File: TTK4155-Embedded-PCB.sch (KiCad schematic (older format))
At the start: 48 parts, among them J1 AVR-JTAG-10, J2 DB9_Female, J3 Conn_01x10_Male, J4 Conn_01x04_Male, J5 Screw_Terminal_01x02, J6 Screw_Terminal_01x02, J7 Conn_01x04_Male, J8 BannanaJack, SW1 SW_Push, U1 L7805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

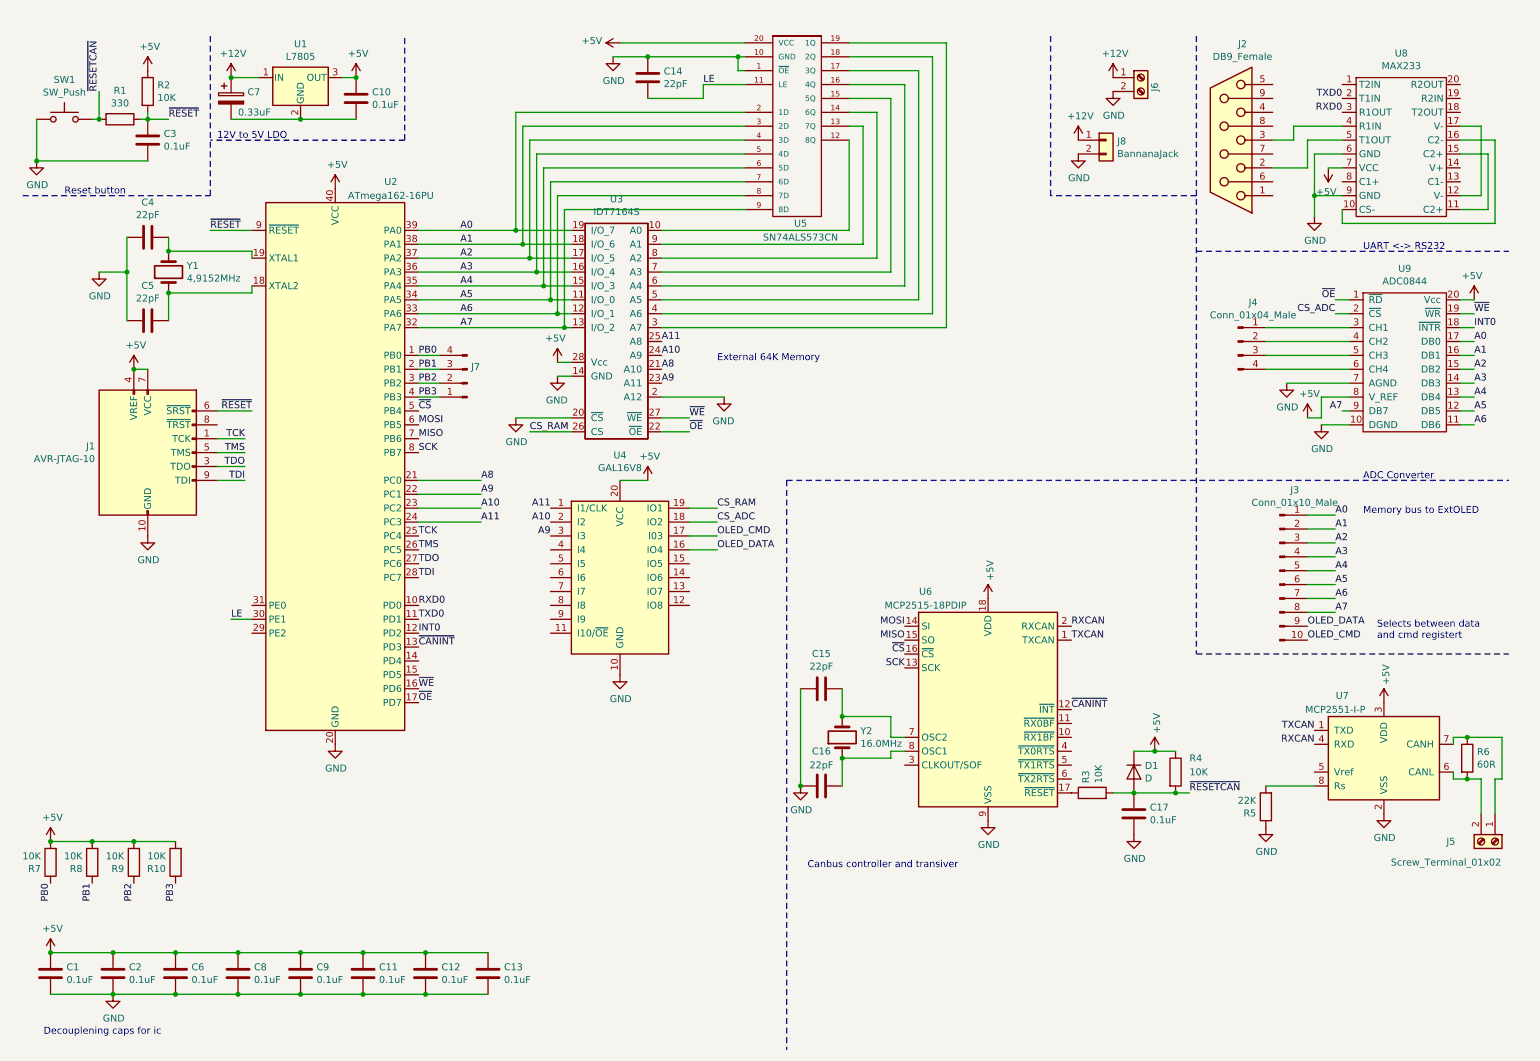
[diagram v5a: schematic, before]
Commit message: Fixed schematics to reflects bodges in rev 1
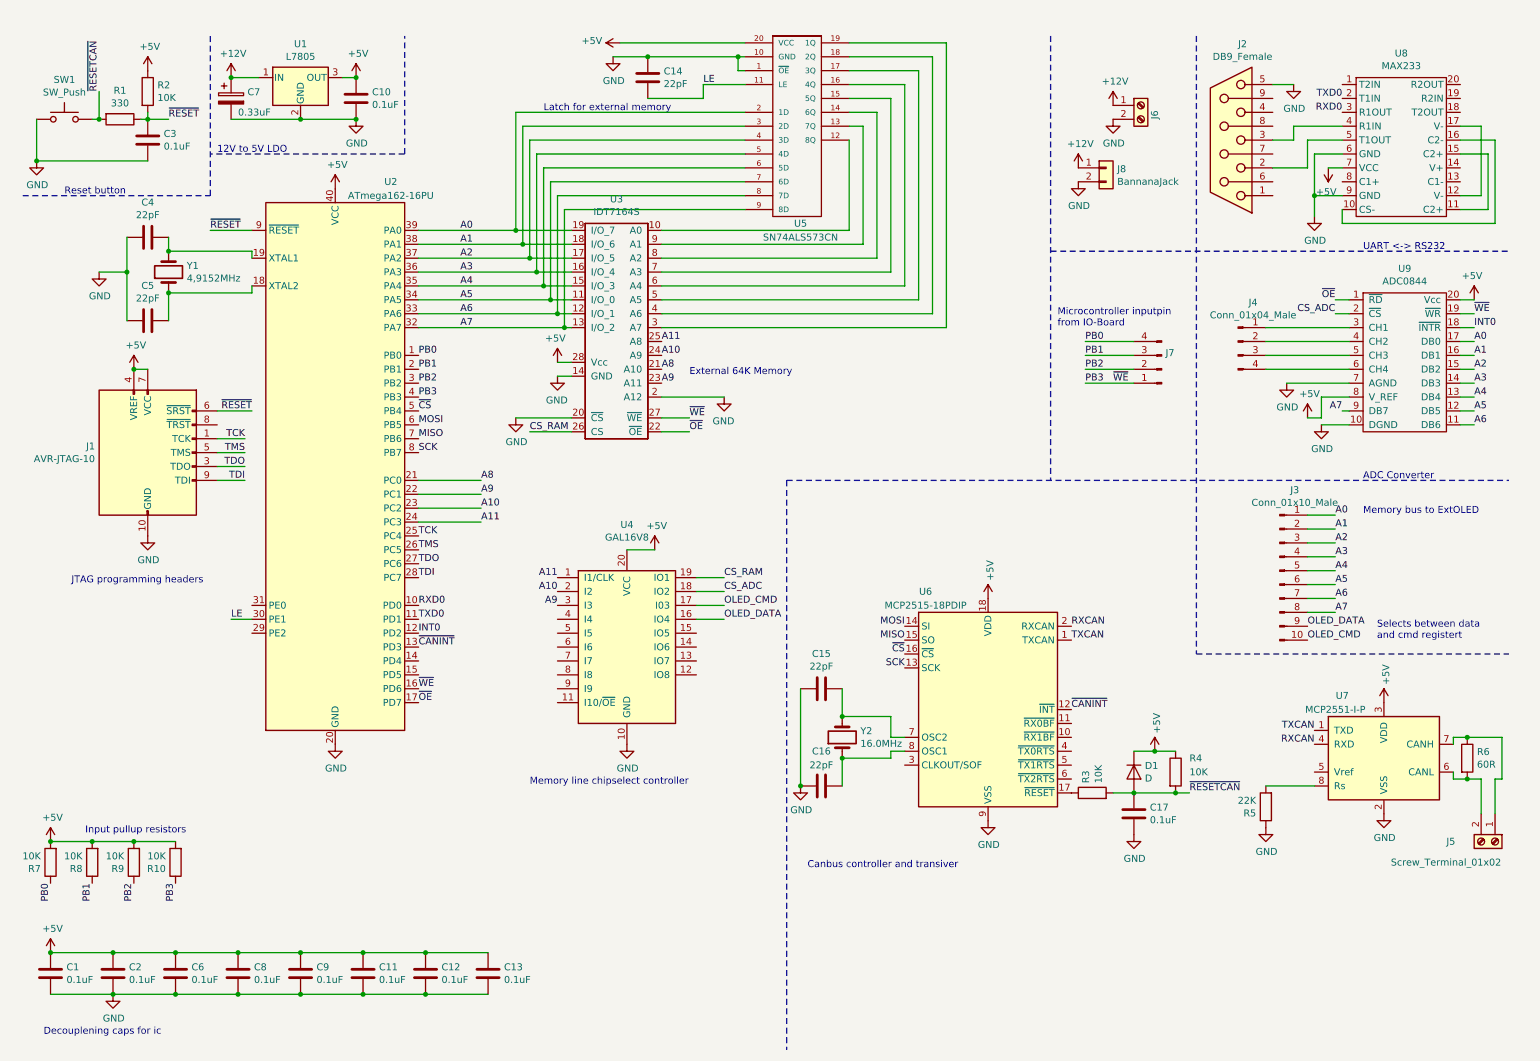
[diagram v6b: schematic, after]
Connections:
- net ~WE is gone; now on net PB3: U2.16 (PD6), U3.27 (~WE), U9.19 (~WR)
- net GND: now also C10.2, C7.2, J2.5, U1.2 (GND)
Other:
- note added: "Input pullup resistors"
- note added: "JTAG programming headers"
- note added: "Latch for external memory"
- note added: "Memory line chipselect controller\n"
- note added: "Microcontroller inputpin \nfrom IO-Board"
- moved on the sheet: J6, J7, J8, U4
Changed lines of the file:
@@
 EESchema Schematic File Version 4
 LIBS:TTK4155-Embedded-PCB-cache
-EELAYER 29 0
+EELAYER 30 0
 EELAYER END
 $Descr A4 11693 8268
@@
 L power:+5V #PWR0116
 U 1 1 5D9B7D1E
-P 5000 3700
-F 0 "#PWR0116" H 5000 3550 50  0001 C CNN
-F 1 "+5V" H 5015 3873 50  0000 C CNN
-F 2 "" H 5000 3700 50  0001 C CNN
-F 3 "" H 5000 3700 50  0001 C CNN
-	1    5000 3700
-	1    0    0    -1
-$EndComp
-Wire Wire Line
-	5500 3900 5300 3900
+P 5050 4200
+F 0 "#PWR0116" H 5050 4050 50  0001 C CNN
+F 1 "+5V" H 5065 4373 50  0000 C CNN
+F 2 "" H 5050 4200 50  0001 C CNN
+F 3 "" H 5050 4200 50  0001 C CNN
+	1    5050 4200
+	1    0    0    -1
+$EndComp
+Wire Wire Line
+	5550 4400 5350 4400
 $Comp
 L power:GND #PWR0117
 U 1 1 5D9BFE96
-P 4800 5100
-F 0 "#PWR0117" H 4800 4850 50  0001 C CNN
-F 1 "GND" H 4805 4927 50  0000 C CNN
-F 2 "" H 4800 5100 50  0001 C CNN
-F 3 "" H 4800 5100 50  0001 C CNN
-	1    4800 5100
+P 4850 5600
+F 0 "#PWR0117" H 4850 5350 50  0001 C CNN
+F 1 "GND" H 4855 5427 50  0000 C CNN
+F 2 "" H 4850 5600 50  0001 C CNN
+F 3 "" H 4850 5600 50  0001 C CNN
+	1    4850 5600
 	1    0    0    -1
 $EndComp
@@
 Wire Wire Line
 	5650 650  5700 650
-Text Label 5500 3900 0    50   ~ 0
+Text Label 5550 4400 0    50   ~ 0
 CS_RAM
 Text Label 4150 3350 0    50   ~ 0
@@
 L Logic_Programmable:GAL16V8 U4
 U 1 1 5D9608E7
-P 4800 4400
-F 0 "U4" H 4800 5281 50  0000 C CNN
-F 1 "GAL16V8" H 4800 5190 50  0000 C CNN
-F 2 "Package_DIP:DIP-20_W7.62mm_Socket_LongPads" H 4800 4400 50  0001 C CNN
-F 3 "" H 4800 4400 50  0001 C CNN
-	1    4800 4400
+P 4850 4900
+F 0 "U4" H 4850 5781 50  0000 C CNN
+F 1 "GAL16V8" H 4850 5690 50  0000 C CNN
+F 2 "Package_DIP:DIP-20_W7.62mm_Socket_LongPads" H 4850 4900 50  0001 C CNN
+F 3 "" H 4850 4900 50  0001 C CNN
+	1    4850 4900
 	1    0    0    -1
 $EndComp
@@
 Text Label 3800 4000 0    50   ~ 0
 A11
-Wire Notes Line
-	8950 2050 11200 2050
 Text Notes 10150 2050 0    50   ~ 0
 UART <-> RS232
-Text Notes 5500 2850 0    50   ~ 0
+Text Notes 5300 2950 0    50   ~ 0
 External 64K Memory
 $Comp
@@
 Reset button
 Wire Notes Line
-	3250 1250 3250 500
-Text Notes 1900 1250 0    50   ~ 0
+	3250 1350 3250 500
+Text Notes 1900 1350 0    50   ~ 0
 12V to 5V LDO
 $Comp
@@
 INT0
 Wire Wire Line
-	5300 4000 5500 4000
-Text Label 5500 4000 0    50   ~ 0
+	5350 4500 5550 4500
+Text Label 5550 4500 0    50   ~ 0
 CS_ADC
 Text Label 9950 2500 2    50   ~ 0
@@
 Memory bus to ExtOLED
 Wire Wire Line
-	5300 4100 5500 4100
-Wire Wire Line
-	5300 4200 5500 4200
-Text Label 5500 4100 0    50   ~ 0
+	5350 4600 5550 4600
+Wire Wire Line
+	5350 4700 5550 4700
+Text Label 5550 4600 0    50   ~ 0
 OLED_CMD
-Text Label 5500 4200 0    50   ~ 0
+Text Label 5550 4700 0    50   ~ 0
 OLED_DATA
 Text Label 9750 4850 0    50   ~ 0
@@
 Selects between data \nand cmd registert\n
 Wire Wire Line
-	4800 3700 5000 3700
+	4850 4200 5050 4200
 Wire Wire Line
 	4800 550  5700 550
@@
 Wire Wire Line
 	3350 3700 3800 3700
-Text Label 4300 3900 2    50   ~ 0
+Text Label 4350 4400 2    50   ~ 0
 A11
-Text Label 4300 4000 2    50   ~ 0
+Text Label 4350 4500 2    50   ~ 0
 A10
-Text Label 4300 4100 2    50   ~ 0
+Text Label 4350 4600 2    50   ~ 0
 A9
 $Comp
@@
 L Connector:Screw_Terminal_01x02 J6
 U 1 1 5DD11A7E
-P 8550 800
-F 0 "J6" V 8650 700 50  0000 L CNN
-F 1 "Screw_Terminal_01x02" V 8750 200 50  0001 L CNN
-F 2 "TerminalBlock_MetzConnect:TerminalBlock_MetzConnect_Type073_RT02602HBLU_1x02_P5.08mm_Horizontal" H 8550 800 50  0001 C CNN
-F 3 "~" H 8550 800 50  0001 C CNN
-	1    8550 800
+P 8550 1000
+F 0 "J6" V 8650 900 50  0000 L CNN
+F 1 "Screw_Terminal_01x02" V 8750 400 50  0001 L CNN
+F 2 "TerminalBlock_MetzConnect:TerminalBlock_MetzConnect_Type073_RT02602HBLU_1x02_P5.08mm_Horizontal" H 8550 1000 50  0001 C CNN
+F 3 "~" H 8550 1000 50  0001 C CNN
+	1    8550 1000
 	1    0    0    -1
 $EndComp
@@
 L power:GND #PWR0134
 U 1 1 5DD5A4AB
-P 8350 900
-F 0 "#PWR0134" H 8350 650 50  0001 C CNN
-F 1 "GND" H 8355 727 50  0000 C CNN
-F 2 "" H 8350 900 50  0001 C CNN
-F 3 "" H 8350 900 50  0001 C CNN
-	1    8350 900
+P 8350 1100
+F 0 "#PWR0134" H 8350 850 50  0001 C CNN
+F 1 "GND" H 8355 927 50  0000 C CNN
+F 2 "" H 8350 1100 50  0001 C CNN
+F 3 "" H 8350 1100 50  0001 C CNN
+	1    8350 1100
 	1    0    0    -1
 $EndComp
@@
 L power:+12V #PWR0135
 U 1 1 5DDD0920
-P 8350 800
-F 0 "#PWR0135" H 8350 650 50  0001 C CNN
-F 1 "+12V" H 8365 973 50  0000 C CNN
-F 2 "" H 8350 800 50  0001 C CNN
-F 3 "" H 8350 800 50  0001 C CNN
-	1    8350 800
+P 8350 1000
+F 0 "#PWR0135" H 8350 850 50  0001 C CNN
+F 1 "+12V" H 8365 1173 50  0000 C CNN
+F 2 "" H 8350 1000 50  0001 C CNN
+F 3 "" H 8350 1000 50  0001 C CNN
+	1    8350 1000
 	1    0    0    -1
 $EndComp
@@
 L Connector:Conn_01x04_Male J7
 U 1 1 5DDF74B0
-P 3700 3000
-F 0 "J7" H 3672 2882 50  0000 R CNN
-F 1 "Conn_01x04_Male" H 3672 2973 50  0001 R CNN
-F 2 "Connector_PinHeader_2.54mm:PinHeader_1x04_P2.54mm_Vertical" H 3700 3000 50  0001 C CNN
-F 3 "~" H 3700 3000 50  0001 C CNN
-	1    3700 3000
+P 8700 2900
+F 0 "J7" H 8672 2782 50  0000 R CNN
+F 1 "Conn_01x04_Male" H 8672 2873 50  0001 R CNN
+F 2 "Connector_PinHeader_2.54mm:PinHeader_1x04_P2.54mm_Vertical" H 8700 2900 50  0001 C CNN
+F 3 "~" H 8700 2900 50  0001 C CNN
+	1    8700 2900
 	-1   0    0    1
 $EndComp
 Wire Notes Line
-	3250 1250 1850 1250
+	3250 1350 1850 1350
 $Comp
 L Connector_Generic:Conn_01x02 J8
 U 1 1 5DE8CCC3
-P 8300 1250
-F 0 "J8" H 8380 1242 50  0000 L CNN
-F 1 "BannanaJack" H 8380 1151 50  0000 L CNN
-F 2 "TTK4155-Embedded-PCB:Banana_Jack_2Pin_15mm_spacing" H 8300 1250 50  0001 C CNN
-F 3 "~" H 8300 1250 50  0001 C CNN
-	1    8300 1250
+P 8300 1450
+F 0 "J8" H 8380 1442 50  0000 L CNN
+F 1 "BannanaJack" H 8380 1351 50  0000 L CNN
+F 2 "TTK4155-Embedded-PCB:Banana_Jack_2Pin_15mm_spacing" H 8300 1450 50  0001 C CNN
+F 3 "~" H 8300 1450 50  0001 C CNN
+	1    8300 1450
 	1    0    0    -1
 $EndComp
@@
 L power:GND #PWR0136
 U 1 1 5DE9BBA9
-P 8100 1350
-F 0 "#PWR0136" H 8100 1100 50  0001 C CNN
-F 1 "GND" H 8105 1177 50  0000 C CNN
-F 2 "" H 8100 1350 50  0001 C CNN
-F 3 "" H 8100 1350 50  0001 C CNN
-	1    8100 1350
+P 8100 1550
+F 0 "#PWR0136" H 8100 1300 50  0001 C CNN
+F 1 "GND" H 8105 1377 50  0000 C CNN
+F 2 "" H 8100 1550 50  0001 C CNN
+F 3 "" H 8100 1550 50  0001 C CNN
+	1    8100 1550
 	1    0    0    -1
 $EndComp
@@
 L power:+12V #PWR0137
 U 1 1 5DEE3528
-P 8100 1250
-F 0 "#PWR0137" H 8100 1100 50  0001 C CNN
-F 1 "+12V" H 8115 1423 50  0000 C CNN
-F 2 "" H 8100 1250 50  0001 C CNN
-F 3 "" H 8100 1250 50  0001 C CNN
-	1    8100 1250
-	1    0    0    -1
-$EndComp
-Wire Notes Line
-	8950 1650 7900 1650
-Wire Notes Line
-	7900 1650 7900 500
+P 8100 1450
+F 0 "#PWR0137" H 8100 1300 50  0001 C CNN
+F 1 "+12V" H 8115 1623 50  0000 C CNN
+F 2 "" H 8100 1450 50  0001 C CNN
+F 3 "" H 8100 1450 50  0001 C CNN
+	1    8100 1450
+	1    0    0    -1
+$EndComp
 $Comp
 L Device:R R7
@@
 Text Label 3350 3100 0    50   ~ 0
 PB3
-Wire Wire Line
-	3350 2800 3500 2800
-Wire Wire Line
-	3350 2900 3500 2900
-Wire Wire Line
-	3350 3000 3500 3000
-Wire Wire Line
-	3350 3100 3500 3100
 $Comp
 L Device:R R8
@@
 Text Label 1600 6600 3    50   ~ 0
 PB3
+$Comp
+L power:GND #PWR?
+U 1 1 5DD0858E
+P 9650 850
+F 0 "#PWR?" H 9650 600 50  0001 C CNN
+F 1 "GND" H 9655 677 50  0000 C CNN
+F 2 "" H 9650 850 50  0001 C CNN
+F 3 "" H 9650 850 50  0001 C CNN
+	1    9650 850
+	1    0    0    -1
+$EndComp
+Wire Wire Line
+	9650 850  9500 850
+$Comp
+L power:GND #PWR?
+U 1 1 5DD37A87
+P 2900 1100
+F 0 "#PWR?" H 2900 850 50  0001 C CNN
+F 1 "GND" H 2905 927 50  0000 C CNN
+F 2 "" H 2900 1100 50  0001 C CNN
+F 3 "" H 2900 1100 50  0001 C CNN
+	1    2900 1100
+	1    0    0    -1
+$EndComp
+Connection ~ 2900 1100
+Text Label 8350 3000 0    50   ~ 0
+~WE
+Wire Wire Line
+	8150 3000 8500 3000
+Wire Wire Line
+	8150 2900 8500 2900
+Wire Wire Line
+	8150 2800 8500 2800
+Wire Wire Line
+	8150 2700 8500 2700
+Text Notes 4150 5900 0    50   ~ 0
+Memory line chipselect controller\n
+Text Notes 850  4450 0    50   ~ 0
+JTAG programming headers
+Text Notes 4250 1050 0    50   ~ 0
+Latch for external memory
+Text Notes 950  6250 0    50   ~ 0
+Input pullup resistors
+Text Label 8150 2700 0    50   ~ 0
+PB0
+Text Label 8150 2800 0    50   ~ 0
+PB1
+Text Label 8150 2900 0    50   ~ 0
+PB2
+Text Label 8150 3000 0    50   ~ 0
+PB3
+Wire Notes Line
+	7900 500  7900 3700
+Text Notes 7950 2600 0    50   ~ 0
+Microcontroller inputpin \nfrom IO-Board
+Wire Notes Line
+	7900 2050 11200 2050
 $EndSCHEMATC
